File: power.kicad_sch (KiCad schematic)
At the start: 41 parts, among them U1 74HC86, U10 74AHC30, U11 74AHC30, U12 74AHC30, U13 74AHC30, U15 74LV32, U16 74HC109, U17 74LV32, U18 74LV04, U19 74LV08, U2 74HC00, U21 74AHC30, U22 74AHC30, U23 74AHC30, U24 74AHC30, U25 74HC109, U3 74LV27, U30 74LV08, U31 74LV08, U4 74HC00

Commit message: Memory routing *screams*
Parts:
- U16, U25: value 74HC109 -> 74AC109
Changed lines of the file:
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@@
       (effects (font (size 1.27 1.27)) (justify left))
     )
-    (property "Value" "74HC109" (at 166.37 118.11 0)
+    (property "Value" "74AC109" (at 166.37 118.11 0)
       (effects (font (size 1.27 1.27)) (justify left))
     )
@@
       (effects (font (size 1.27 1.27)) (justify left))
     )
-    (property "Value" "74HC109" (at 189.23 118.11 0)
-      (effects (font (size 1.27 1.27)) (justify left))
-    )
+    (property "Value" "74AC109" (at 189.23 118.11 0)
+      (effects (font (size 1.27 1.27)) (justify left))
+    )

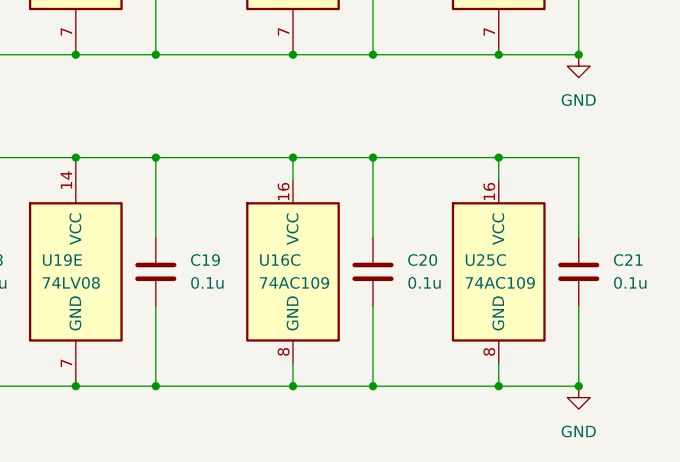
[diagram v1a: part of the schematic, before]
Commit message: Suuuper dense routing for column counter
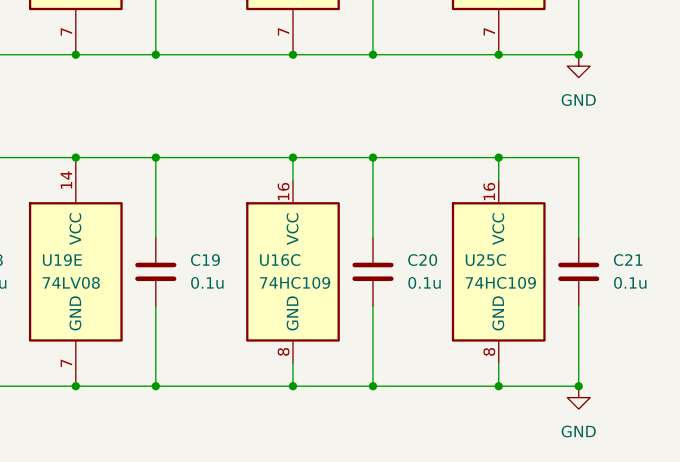
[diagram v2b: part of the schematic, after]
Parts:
- U16, U25: value 74AC109 -> 74HC109
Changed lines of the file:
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@@
       (effects (font (size 1.27 1.27)) (justify left))
     )
-    (property "Value" "74AC109" (at 166.37 118.11 0)
+    (property "Value" "74HC109" (at 166.37 118.11 0)
       (effects (font (size 1.27 1.27)) (justify left))
     )
@@
       (effects (font (size 1.27 1.27)) (justify left))
     )
-    (property "Value" "74AC109" (at 189.23 118.11 0)
-      (effects (font (size 1.27 1.27)) (justify left))
-    )
+    (property "Value" "74HC109" (at 189.23 118.11 0)
+      (effects (font (size 1.27 1.27)) (justify left))
+    )
